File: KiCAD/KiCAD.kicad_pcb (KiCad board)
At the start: 2 copper layers, 112.1 x 150 mm, 147 parts, among them J1 Conn_01x02_Pin, J13 Conn_01x05, J15 Conn_01x03_Pin, J16 Conn_01x05, J4 8P8C_Shielded, J5 ENC_INT if needed, J6 TX/RX, J7 HV, J8 HV_INRUSH_BYPASS, J9 TR_SENSE, Q1 J310, Q4 2N7000, Q5 2N7000, Q6 2N7000, Q7 2N7000, T1 2N3906, T2 2N3906, U1 Si5351A_Breakout, U15 LM7805_TO220, U16 AM26LS32ACN, U17 Adafruit_PCF8575_Breakout, U18 CD14538B, U19 L79L08_TO92, U20 ICL7660S, U3 MC1496, U4 MCP4921, U6 LM7171xIN, U7 LM7171xIN, U8 MCP4728

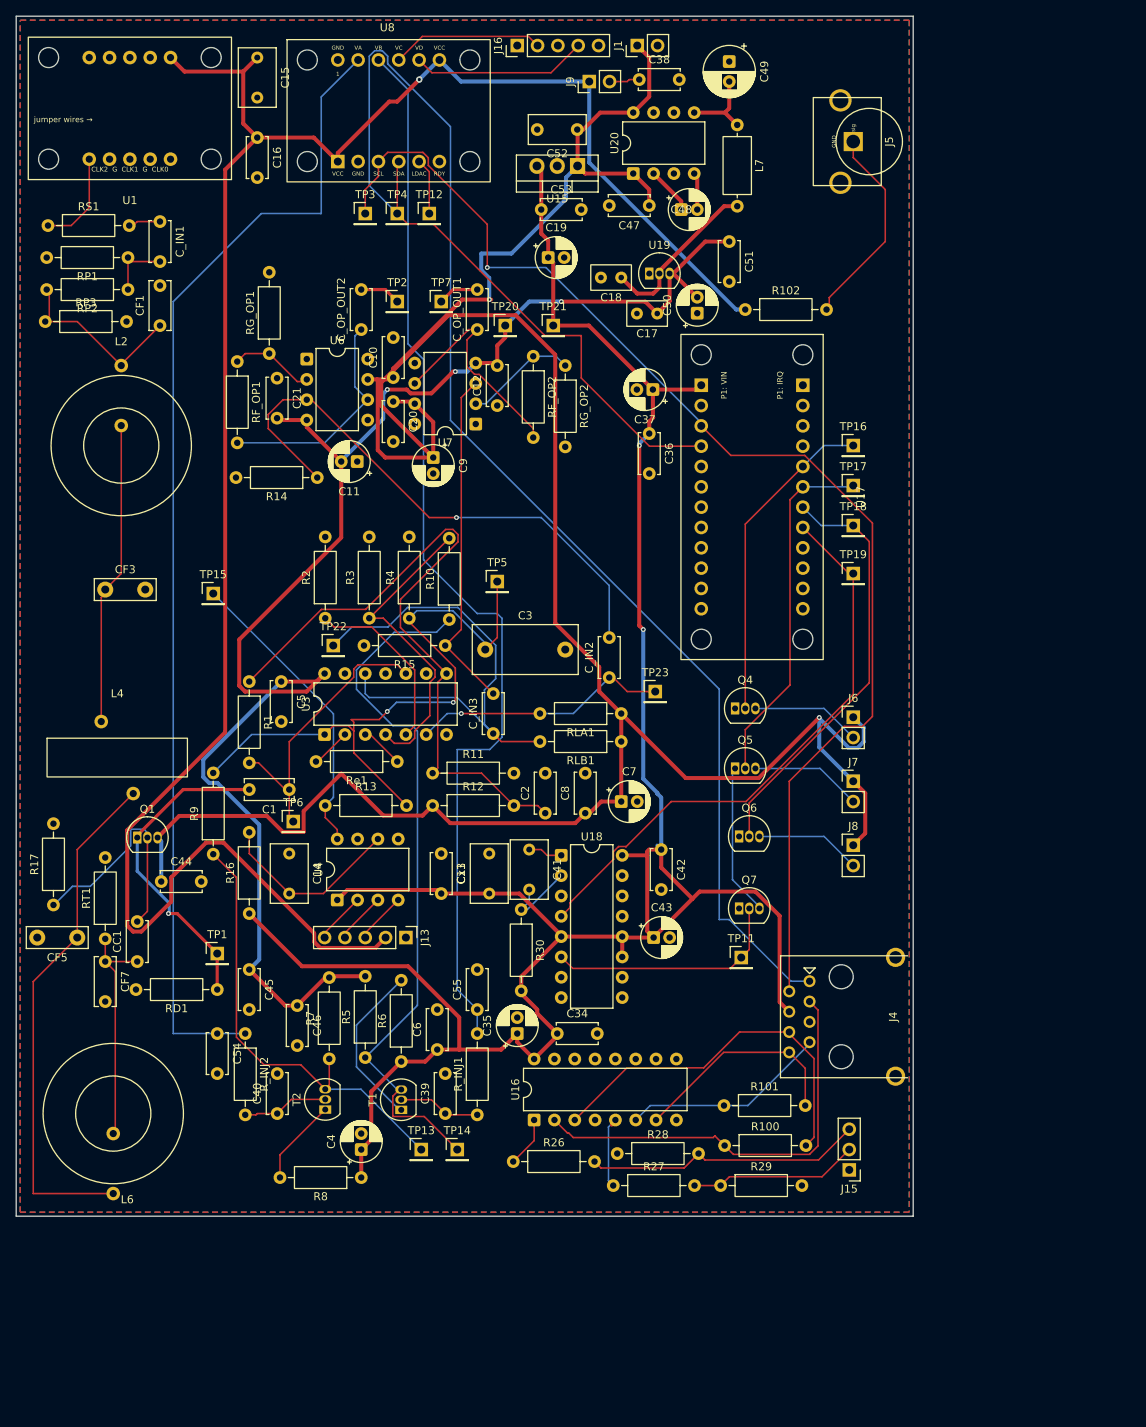
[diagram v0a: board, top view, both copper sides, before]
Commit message: kicad: expand board to 130x170mm, 4 corner mounting holes, silk cleanup
- Edge.Cuts expanded from 112x150 to 130x170 mm to make room for
  proper corner-inset mounting holes without conflicting with U1
  (Si5351 breakout) or L6 (T68-6 toroid)
- 4 MountingHole_3.2mm_M3 at (11,10), (131,10), (11,170), (131,170)
  with 8+ mm clearance to nearest components
- GND zones resized to match new outline
- RJ45 (J4) repositioned and reconnected on the expanded board
- Silk cleanup: 43 silk_overlap warnings resolved by moving reference
  designators
- min_text_height rule dropped 0.8 -> 0.5 mm to accommodate external
  breakout footprints (U8, U17, J5, U1 silk was intentionally smaller)

DRC: 24 violations remain, all cosmetic silkscreen. No functional
errors (unconnected, clearance, hole-to-hole, starved thermals).

Co-Authored-By: Claude Opus 4.7 <noreply@anthropic.com>
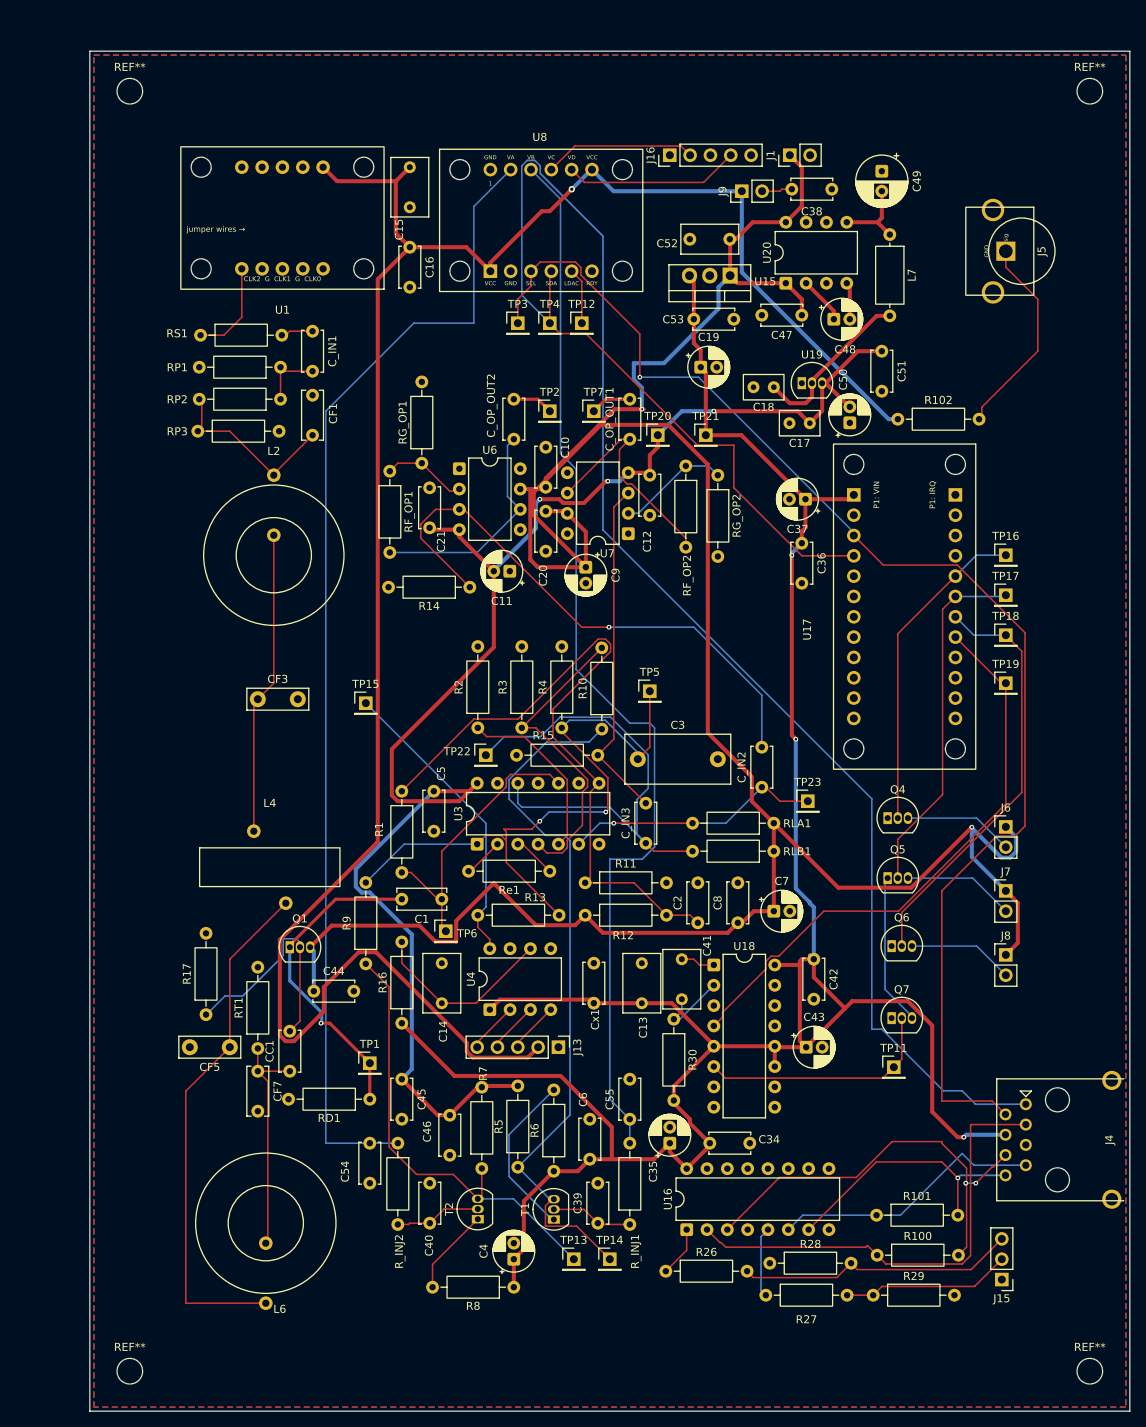
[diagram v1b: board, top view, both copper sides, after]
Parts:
- added REF**: MountingHole_3.2mm_M3, MountingHole:MountingHole_3.2mm_M3, F.Cu at (30.1, 23.7)
- added REF**: MountingHole_3.2mm_M3, MountingHole:MountingHole_3.2mm_M3, F.Cu at (150.1, 23.7)
- added REF**: MountingHole_3.2mm_M3, MountingHole:MountingHole_3.2mm_M3, F.Cu at (30.1, 183.7)
- added REF**: MountingHole_3.2mm_M3, MountingHole:MountingHole_3.2mm_M3, F.Cu at (150.1, 183.7)
- moved J4 31.1 mm to (146.0, 154.8)
- moved R17 23.5 mm to (39.6, 139.1)
- moved R9 23.5 mm to (59.6, 132.8)
- moved C19 23.5 mm to (101.4, 58.2)
- moved C37 23.5 mm to (114.5, 74.7)
- moved J13 23.5 mm to (83.7, 143.2)
- moved U16 23.5 mm to (99.7, 166.0)
- moved U6 23.5 mm to (71.3, 70.9)
- moved C21 23.5 mm to (67.5, 73.3)
- moved C44 23.5 mm to (53.1, 136.2)
- moved C54 23.5 mm to (60.1, 155.2)
- moved CC1 23.5 mm to (50.1, 146.2)
- moved CF3 23.5 mm to (46.1, 99.7)
- moved CF5 23.5 mm to (42.6, 143.2)
- moved CF7 23.5 mm to (46.1, 146.2)
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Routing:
- net +5V: track 296.9 -> 305.8 mm, vias 2 -> 3
- net SDA: track 223.3 -> 231.9 mm
- net SCL: track 156.7 -> 165.4 mm
- net MBL_B_P: track 25.9 -> 34.2 mm
- net MBL_A_N: track 47.3 -> 53.8 mm, vias 0 -> 2
- net MBL_B_N: track 27.6 -> 33.7 mm, vias 0 -> 1
- net MBL_A_P: track 53.8 -> 58.6 mm
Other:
- board size 112.1 x 150 mm -> 130 x 170 mm

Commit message: rev 1: analog control board gerbers submitted to JLCPCB
Order Y2-13077341A, placed 2026-07-14 07:56:41. 5 boards, standard
2-layer FR4 TG135, 1.6mm, 1oz outer copper, HASL, green mask, white
silk, tented vias. Board dimensions 130 x 170 mm. Currently in "Data
Preparation" stage at JLCPCB.

- Add KiCAD/gerber/ folder with the 9 files sent to fab (7 gerber
  layers + Excellon drill + gbrjob metadata) plus the gerber.zip
  actually uploaded. Definitive rev-1 fab artifact.
- Update build_checklist.md Phase 2 with the order record.
- Update pcb_fab_checklist.md current-status snapshot to note rev 1
  submitted, with the rev-2 punch-list items called out (RJ45 pin
  numbering verification, external breakout footprint verification).
- Gitignore: exclude ad-hoc KiCad plot PDFs (KiCAD/KiCAD-*.pdf and
  stray /KiCAD-*.pdf at repo root); they're redundant with the
  gerbers and easily regenerable.

Also folds in incidental schematic/PCB touches (backup of the
routing state at the moment of fab submission) that accumulated
during the plot/gerber generation session.

Co-Authored-By: Claude Opus 4.7 <noreply@anthropic.com>
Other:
- board text added: "Rev A"
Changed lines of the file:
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@@
 		(filling no)
 		(pcbplotparams
-			(layerselection 0x00000000_00000000_55555555_5755f5ff)
+			(layerselection 0x00000000_00000000_55555555_575555ff)
 			(plot_on_all_layers_selection 0x00000000_00000000_00000000_00000000)
 			(disableapertmacros no)
@@
 			(sketchdnponfab yes)
 			(crossoutdnponfab yes)
-			(subtractmaskfromsilk no)
+			(subtractmaskfromsilk yes)
 			(outputformat 1)
 			(mirror no)
-			(drillshape 1)
+			(drillshape 0)
 			(scaleselection 1)
-			(outputdirectory "")
+			(outputdirectory "gerber/")
 		)
 	)
@@
 		(layer "Edge.Cuts")
 	)
+	(gr_text "Rev A"
+		(at 148 94.5 90)
+		(layer "F.SilkS")
+		(effects
+			(font
+				(size 1 1)
+				(thickness 0.15)
+			)
+			(justify left bottom)
+		)
+	)
 	(segment
